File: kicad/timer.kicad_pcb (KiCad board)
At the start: 2 copper layers, 3 parts, among them IC1 ATMEGA328P-A, U1 TOUCH_PAD_15, U2 MTCH6102_SSOP

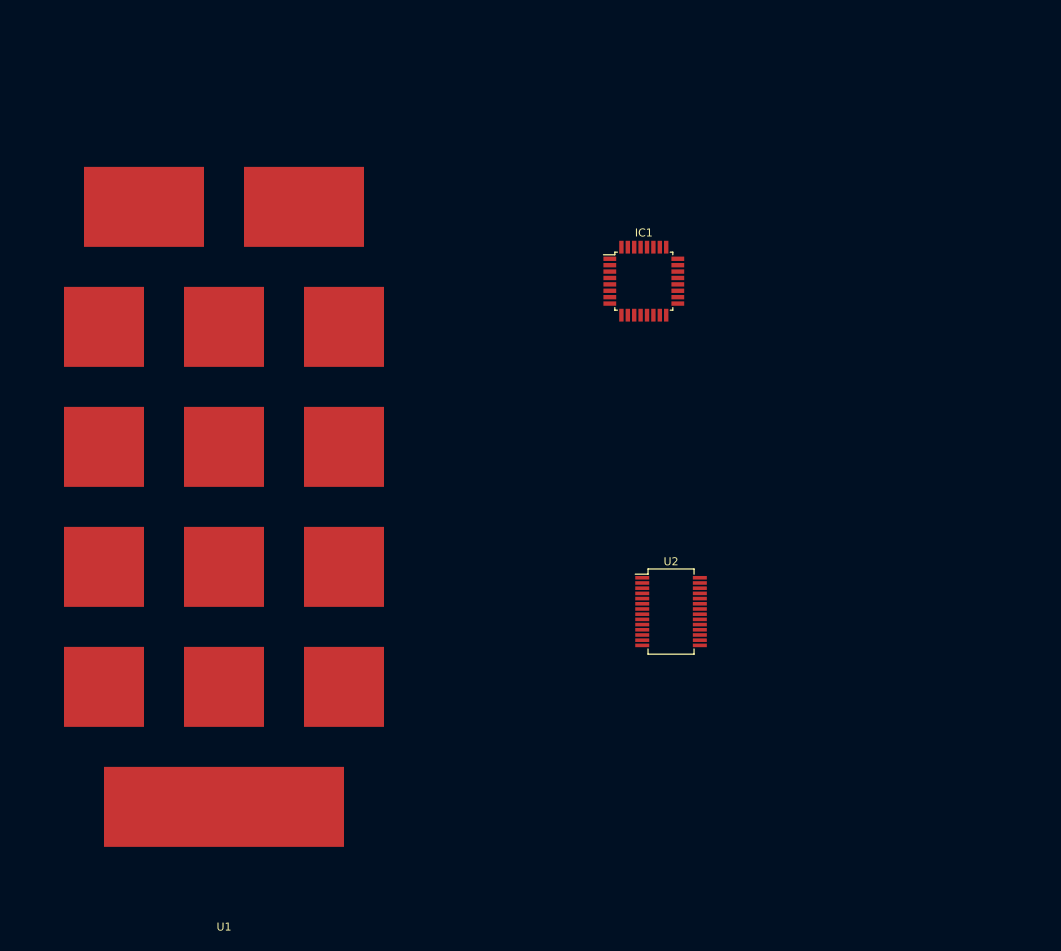
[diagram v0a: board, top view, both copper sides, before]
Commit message: Clock like input
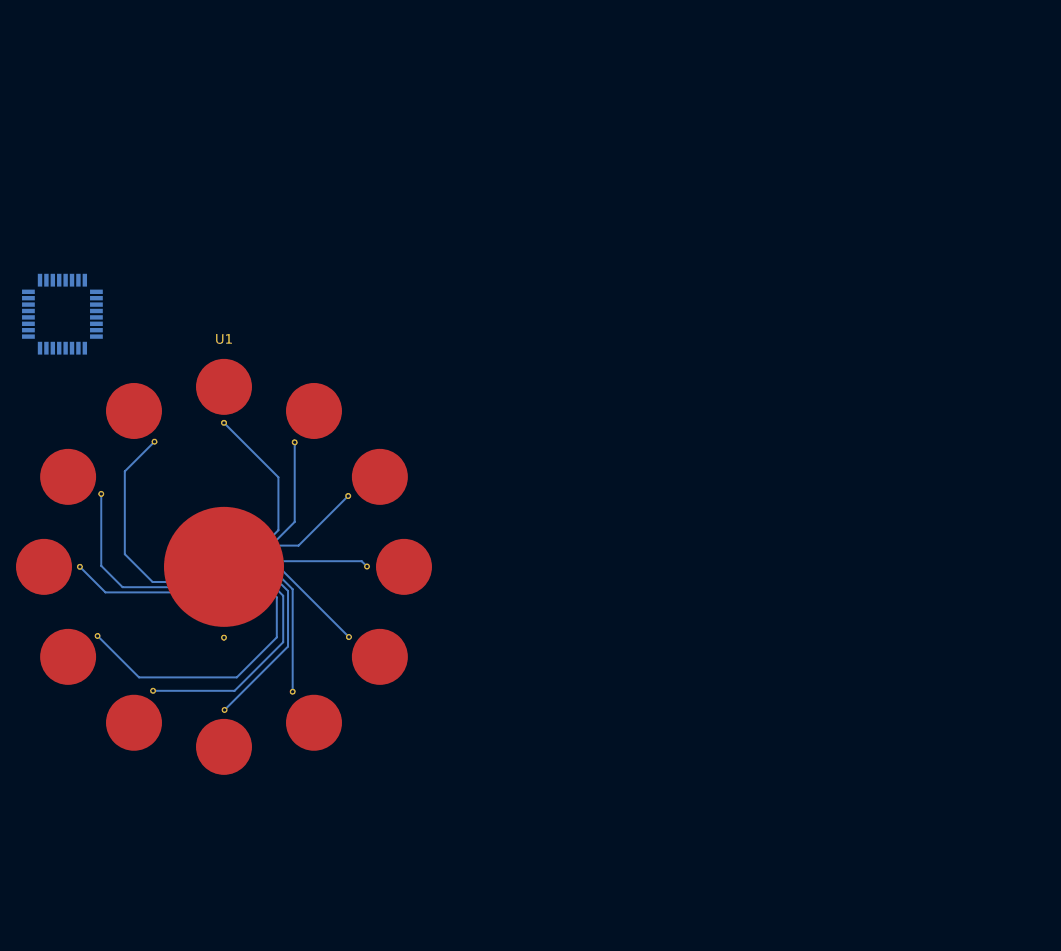
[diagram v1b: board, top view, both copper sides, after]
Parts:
- IC1, U2: moved to B.Cu
- U1: value TOUCH_PAD_15 -> TOUCH_PAD_13; footprint touch_timer:touch_pad_rect -> touch_circle
- moved IC1 72.8 mm to (62.2, 72.2), turned to 180 degrees
- moved U2 56.0 mm to (82.6, 103.4)
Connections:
- U2 pad 13: /RX14 -> Net-(U2-Pad13)
- U2 pad 7: /RX13 -> Net-(U2-Pad7)
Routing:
- net /RX8: track 0.00 -> 34.9 mm
- net /RX7: track 0.00 -> 28.9 mm
- net /RX11: track 0.00 -> 26.0 mm
- net /RX6: track 0.00 -> 23.1 mm
- net /RX10: track 0.00 -> 22.0 mm
- net /RX0: track 0.00 -> 19.6 mm
- net /RX5: track 0.00 -> 18.5 mm
- net /RX1: track 0.00 -> 15.9 mm
- net /RX9: track 0.00 -> 15.9 mm
- net /RX4: track 0.00 -> 15.5 mm
- net /RX3: track 0.00 -> 14.4 mm
- net /RX2: track 0.00 -> 14.3 mm
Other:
- net class Default: via_dia 0.6 -> 0.75
- board text added: "-"
- board text added: "0"
- board text added: "1"
- board text added: "2"
- board text added: "3"
- board text added: "4"
- board text added: "5"
- board text added: "6"
- board text added: "7"
- board text added: "8"
- board text added: "9"
- board text added: "="
- board text added: ">"

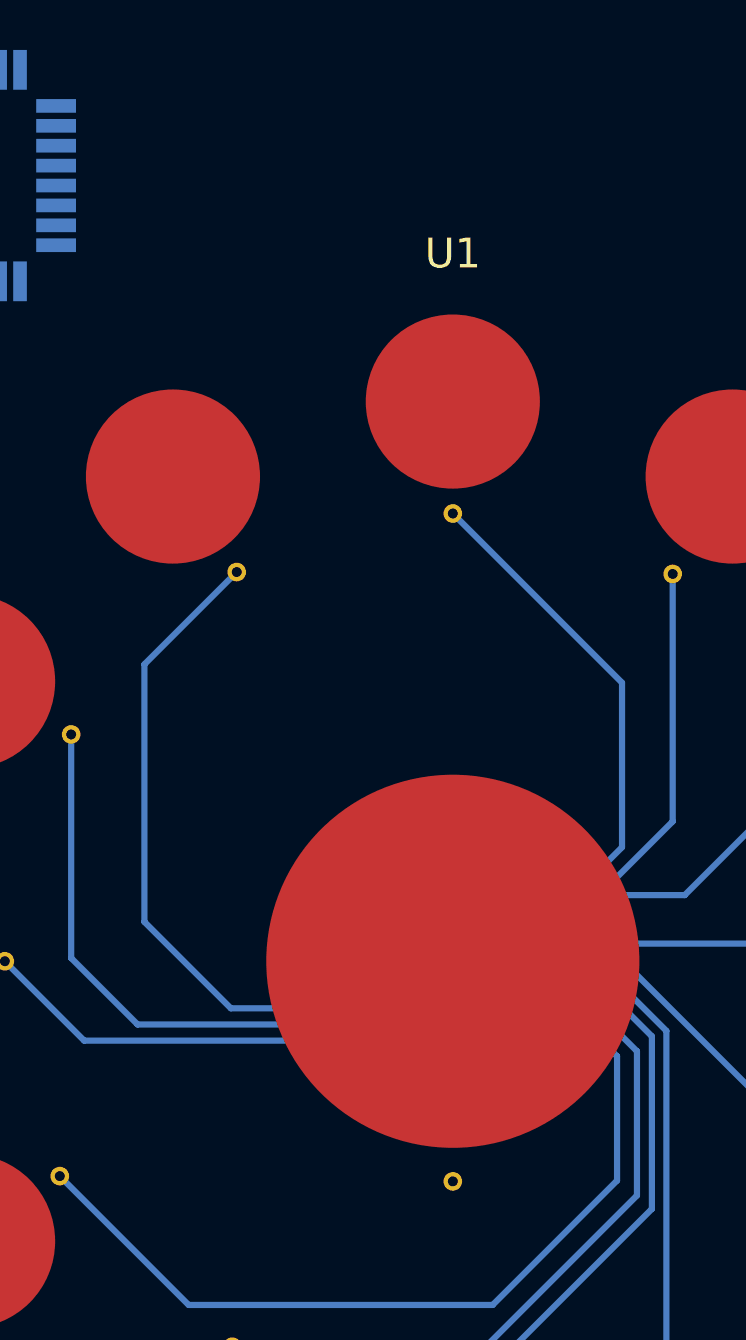
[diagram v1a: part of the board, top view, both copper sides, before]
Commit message: Caps & resistors on the touch ic
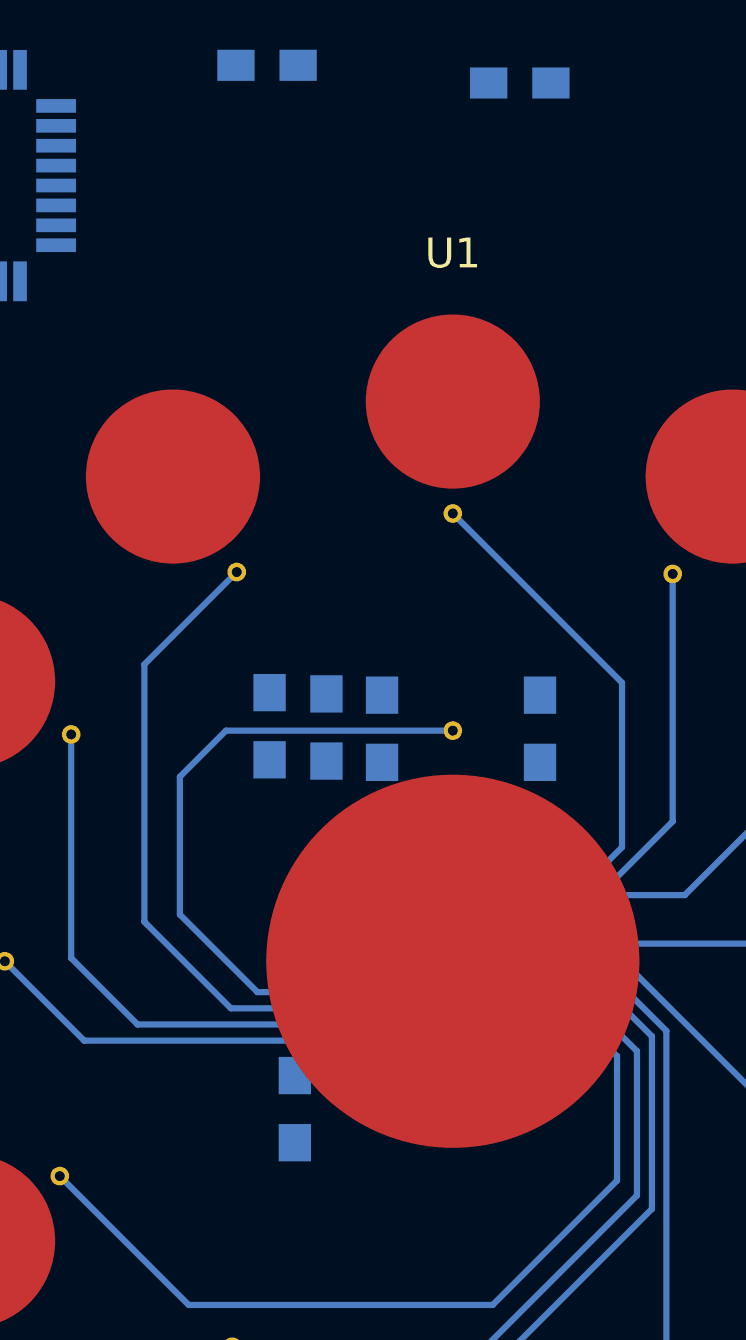
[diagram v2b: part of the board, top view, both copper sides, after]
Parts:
- added C1: 0.1uF, Capacitors_SMD:C_0805_HandSoldering, B.Cu at (74.9, 67.8)
- added C2: 10uF, Capacitors_SMD:C_0805_HandSoldering, B.Cu at (85.1, 68.5)
- added R1: 20k, Resistors_SMD:R_0805_HandSoldering, B.Cu at (76.0, 109.7)
- added R2: 1.8k, Resistors_SMD:R_0805_HandSoldering, B.Cu at (75.0, 94.3)
- added R3: 1.8k, Resistors_SMD:R_0805_HandSoldering, B.Cu at (85.9, 94.4)
- added R4: 4.7k, Resistors_SMD:R_0805_HandSoldering, B.Cu at (77.3, 94.4)
- added R5: 4.7k, Resistors_SMD:R_0805_HandSoldering, B.Cu at (79.6, 94.4)
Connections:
- U2 pad 12: Net-(U2-Pad12) -> /SYNC
- U2 pad 13: Net-(U2-Pad13) -> GND
- U2 pad 19: Net-(U2-Pad19) -> GND
- U2 pad 20: Net-(U2-Pad20) -> VCC
- U2 pad 7: Net-(U2-Pad7) -> GND
- U2 pad 8: Net-(U2-Pad8) -> GND
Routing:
- net /RX12: track 0.00 -> 26.1 mm

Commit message: Layout (wip)
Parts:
- moved R2 4.81 mm to (79.6, 95.8), turned to 180 degrees
- moved R4 3.42 mm to (78.1, 91.1), turned to 180 degrees
- moved R5 1.89 mm to (78.1, 93.2), turned to 180 degrees
- moved R3 1.49 mm to (85.2, 95.8), turned to 0 degrees
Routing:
- net VCC: track 0.00 -> 38.4 mm
- net /RX12: track 26.1 -> 6.01 mm
- net /INT: track 0.00 -> 15.3 mm
- net /SYNC: track 0.00 -> 11.9 mm
- net /SDA: track 0.00 -> 7.26 mm
- net /SCL: track 0.00 -> 6.61 mm
- net /RX10: track 22.0 -> 27.1 mm
- net /RX5: track 18.5 -> 23.5 mm
- net /RX7: track 28.9 -> 33.9 mm
- net /RX2: track 14.3 -> 19.2 mm
- net /RX1: track 15.9 -> 20.9 mm
- net /RX11: track 26.0 -> 30.9 mm
- net /RX4: track 15.5 -> 20.4 mm
- net /RX8: track 34.9 -> 39.7 mm
- net /RX6: track 23.1 -> 27.7 mm
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
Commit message: Sqeeze it in
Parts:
- added C3: 1uF, Capacitors_SMD:C_0805_HandSoldering, B.Cu at (168.0, 62.5)
- added C4: 1uF, Capacitors_SMD:C_0805_HandSoldering, B.Cu at (155.0, 77.0)
- added C5: 0.1uF, Capacitors_SMD:C_0805_HandSoldering, B.Cu at (171.0, 85.0)
- added D1: D_Schottky, Diodes_SMD:SOD-123, B.Cu at (153.0, 42.5)
- added D2: Led, LEDs:LED_0805, B.Cu at (171.0, 80.5)
- added P1: BATTERY, Pin_Headers:Pin_Header_Straight_1x02, B.Cu at (132.0, 42.5)
- added P2: ICSP, Pin_Headers:Pin_Header_Straight_2x03, B.Cu at (122.5, 47.5)
- added Q1: NMOS, TO_SOT_Packages_SMD:SOT-23_Handsoldering, B.Cu at (168.5, 44.0)
- added Q2: PMOS, TO_SOT_Packages_SMD:SOT-23_Handsoldering, B.Cu at (168.5, 51.0)
- added R10: 100k, Resistors_SMD:R_0805_HandSoldering, B.Cu at (167.5, 68.5)
- added R6: 220, Resistors_SMD:R_0805_HandSoldering, B.Cu at (142.0, 76.5)
- added R7: 10K, Resistors_SMD:R_0805_HandSoldering, B.Cu at (165.5, 73.5)
- added R8: 100K, Resistors_SMD:R_0805_HandSoldering, B.Cu at (168.5, 56.0)
- added R9: 820, Resistors_SMD:R_0805_HandSoldering, B.Cu at (172.0, 74.0)
- added SW1: SPST, SMD_Packages:SMD-2010_Pol, B.Cu at (143.5, 42.5)
- added U3: MCP1755ST-3302E/DB, TO_SOT_Packages_SMD:SOT-223, B.Cu at (126.0, 59.0)
- moved C1 91.1 mm to (165.5, 77.5)
- moved IC1 69.4 mm to (130.5, 84.5)
- moved R3 68.0 mm to (153.2, 95.8)
- moved U2 68.0 mm to (150.6, 103.4)
- moved R1 68.0 mm to (144.0, 109.7)
- moved R2 68.0 mm to (147.6, 95.8)
- moved R4 68.0 mm to (146.1, 91.1)
- moved R5 68.0 mm to (146.1, 93.2)
- moved U1 67.6 mm to (150.0, 104.0)
- moved C2 39.0 mm to (123.5, 75.5)
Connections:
- C1 pad 1: VCC -> /3V3
- C2 pad 1: VCC -> /3V3
- IC1 pad 13: Net-(IC1-Pad13) -> /NBASE_ON
- IC1 pad 15: Net-(IC1-Pad15) -> /MOSI
- IC1 pad 16: Net-(IC1-Pad16) -> /MISO
- IC1 pad 17: Net-(IC1-Pad17) -> /SCK
- IC1 pad 21: Net-(IC1-Pad21) -> GND
- IC1 pad 29: Net-(IC1-Pad29) -> /RESET
- IC1 pad 3: Net-(IC1-Pad3) -> GND
- IC1 pad 4: Net-(IC1-Pad4) -> /3V3
- IC1 pad 5: Net-(IC1-Pad5) -> GND
- IC1 pad 6: Net-(IC1-Pad6) -> /3V3
- R1 pad 1: VCC -> /3V3
- R2 pad 1: VCC -> /3V3
- R3 pad 1: VCC -> /3V3
- R4 pad 1: VCC -> Net-(R4-Pad1)
- R5 pad 1: VCC -> /3V3
- U2 pad 20: VCC -> /3V3
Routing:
- net VCC: track 38.4 -> 0.00 mm
- net /3V3: track 0.00 -> 37.1 mm
- net /RX4: track 20.4 -> 23.9 mm
- net /RX1: track 20.9 -> 24.0 mm
- net /RX2: track 19.2 -> 22.2 mm
- net /RX6: track 27.7 -> 29.7 mm
- net Net-(R4-Pad1): track 0.00 -> 1.32 mm
- net /RX7: track 33.9 -> 34.6 mm
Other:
- board outline added: 70 x 100 mm

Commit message: APA_102C
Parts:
- added U4: APA_102C, touch_timer:APA_102C, B.Cu at (125.0, 127.0)
- U1: footprint touch_circle -> touch_timer:touch_circle
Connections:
- IC1 pad 10: Net-(IC1-Pad10) -> /DI
- IC1 pad 11: Net-(IC1-Pad11) -> /CI

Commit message: More squeezing
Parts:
- P1: footprint Pin_Headers:Pin_Header_Straight_1x02 -> Resistors_SMD:R_0805_HandSoldering
- P2: footprint Pin_Headers:Pin_Header_Straight_2x03 -> SIP-6-SMD
- U1: footprint touch_timer:touch_circle -> touch_circle
- moved U3 50.4 mm to (175.0, 47.0)
- moved R6 40.1 mm to (168.0, 46.0)
- moved P2 37.9 mm to (121.4, 85.3), turned to 90 degrees
- moved C2 34.6 mm to (153.0, 93.5)
- moved R7 31.5 mm to (167.0, 42.0)
- moved C4 29.5 mm to (169.0, 51.0), turned to 270 degrees
- moved R8 27.7 mm to (144.0, 43.0)
- moved C1 22.3 mm to (153.0, 96.0)
- moved C5 19.4 mm to (167.1, 66.0), turned to 90 degrees
- moved Q2 19.2 mm to (151.0, 43.0), turned to 270 degrees
- moved D1 15.0 mm to (138.0, 43.0), turned to 180 degrees
- moved D2 15.0 mm to (171.2, 65.5)
- moved SW1 12.5 mm to (131.0, 43.0), turned to 180 degrees
- moved R10 11.1 mm to (178.3, 71.1), turned to 90 degrees
- moved C3 11.0 mm to (175.0, 54.0), turned to 180 degrees
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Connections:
- R4 pad 1: Net-(R4-Pad1) -> /3V3
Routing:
- net /RX12: track 6.01 -> 15.0 mm
- net /SCL: track 6.61 -> 13.4 mm
- net /RX0: track 24.0 -> 26.8 mm
- net GND: track 0.00 -> 2.50 mm
- net Net-(R4-Pad1): track 1.32 -> 0.00 mm
- net /RX11: track 30.6 -> 31.3 mm
